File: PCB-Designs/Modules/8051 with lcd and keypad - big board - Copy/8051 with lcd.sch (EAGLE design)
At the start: 45 parts, among them IC1 AT89S51, IC2 7805TV

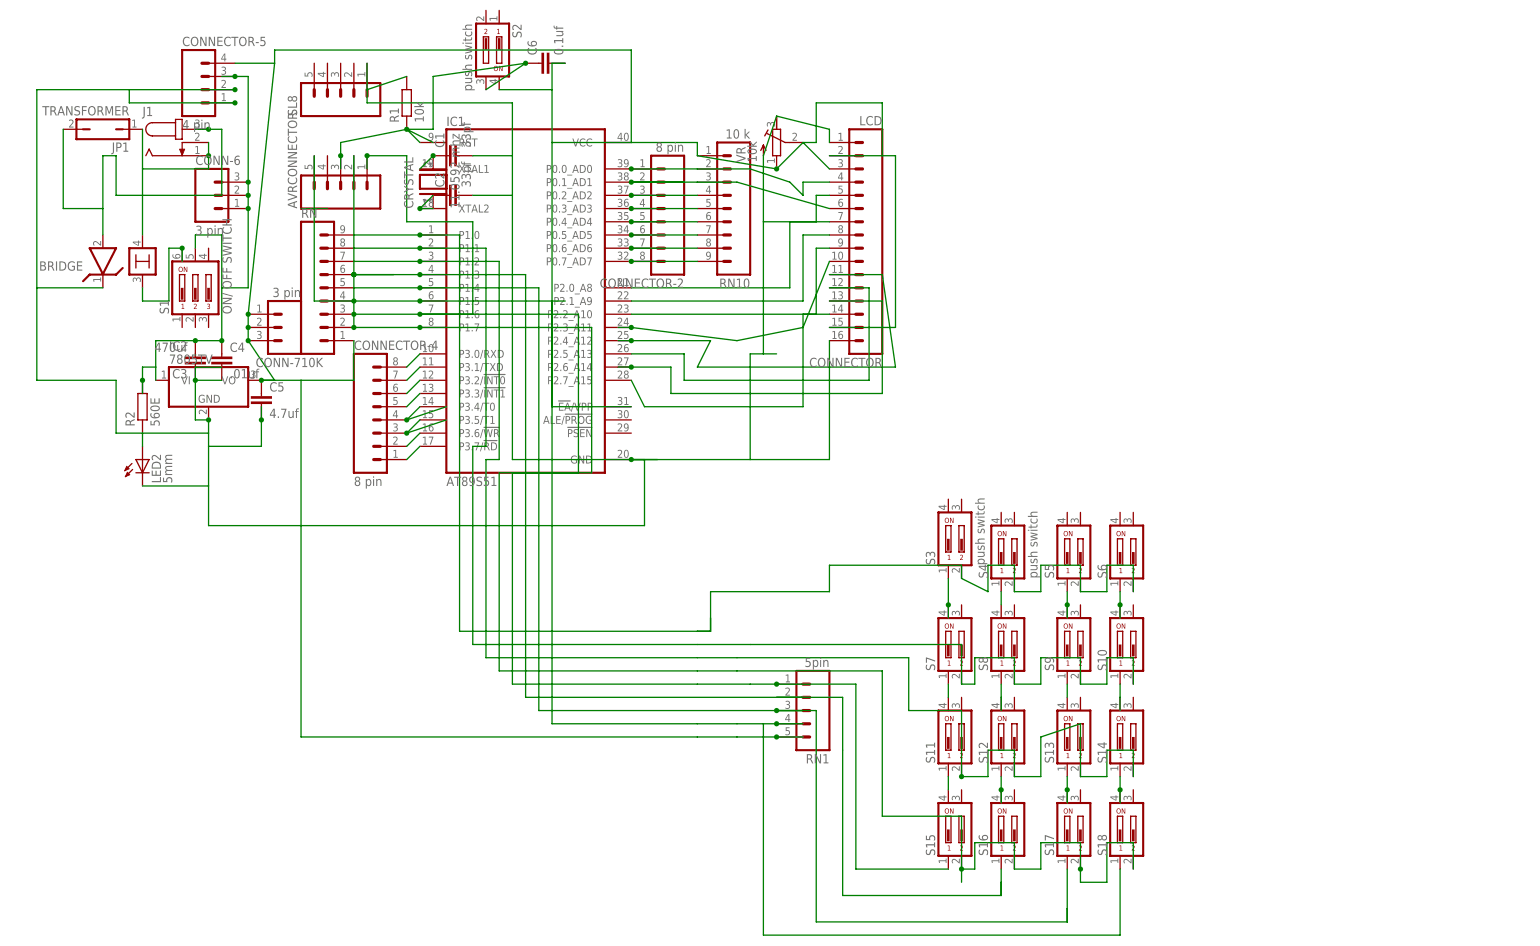
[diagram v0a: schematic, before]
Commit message: 
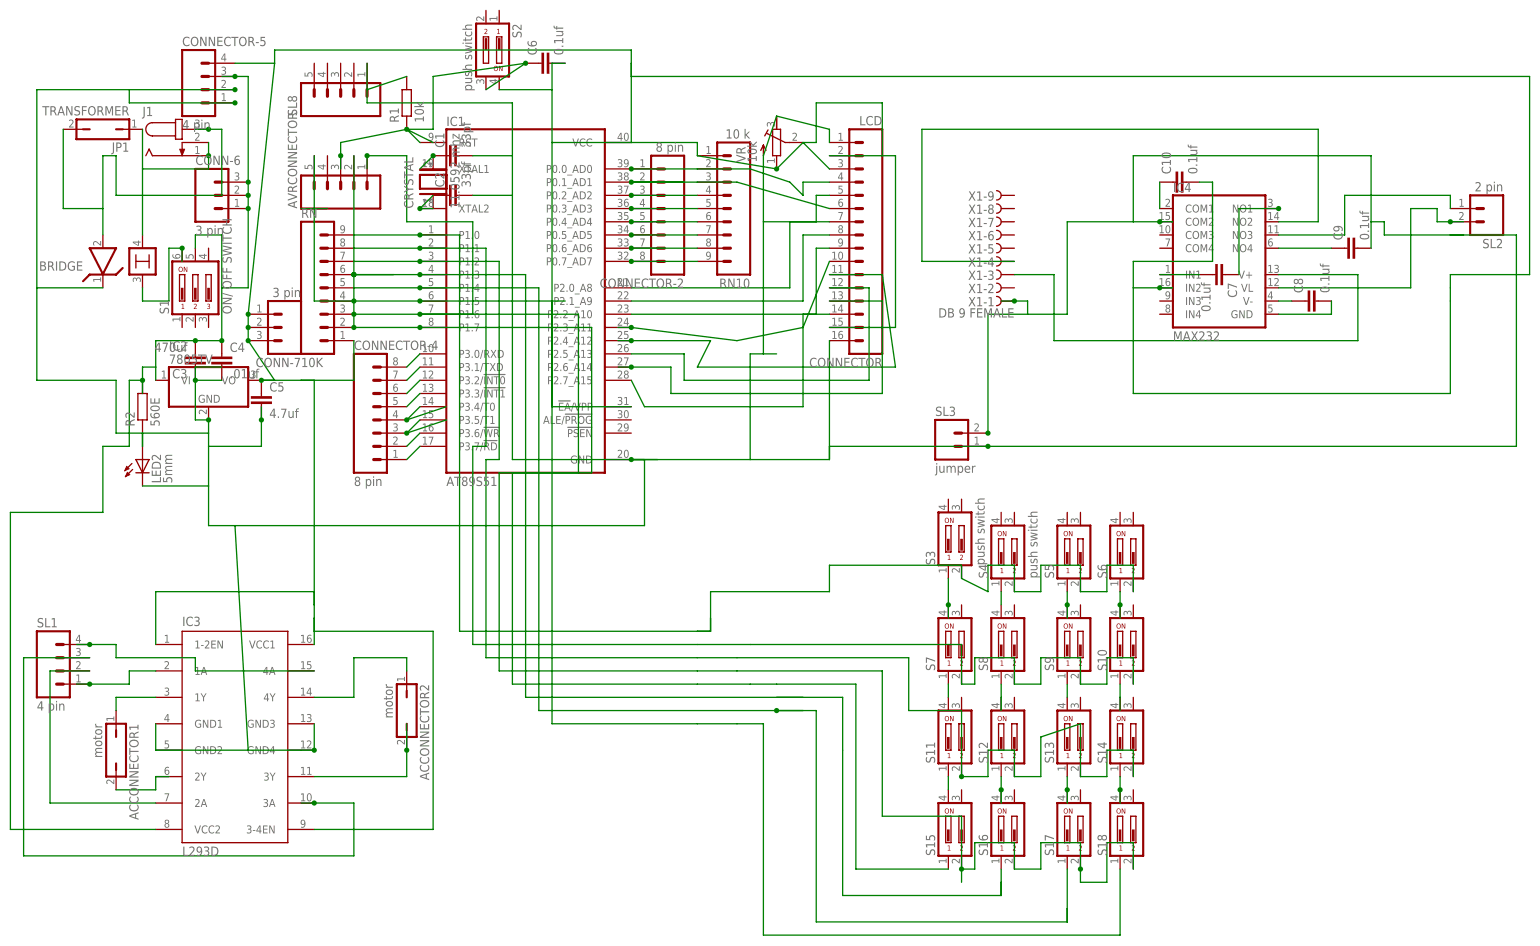
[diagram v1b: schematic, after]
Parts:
- removed RN1: 5pin, con-amp-quick:M05
- added ACCONNECTOR1, ACCONNECTOR2: motor, jumper:JP1Q
- added C10, C7, C8, C9: 0.1uf, capacitor-wima:C2,5-3
- added IC3: L293D, st-microelectronics:L293D
- added IC4: MAX232, maxim:MAX313EPE
- added SL1: 4 pin, con-amp-quick:M04
- added SL2: 2 pin, con-amp-quick:M02
- added SL3: jumper, con-amp-quick:M02
- added X1: DB 9 FEMALE, con-thomas-betts:D-SUB9-H2M09ST
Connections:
- removed net N$39: C5.1, C6.2, CONN-7.1, CONN-7.2, CONN-7.3, CONNECTOR-5.4, CONNECTOR.15, CONNECTOR.2, IC1.!EA!/VPP, IC1.VCC, IC2.VO, RN.1, RN1.5, RN10.1, S2.4, VR.E
- new net N$23: C7.1, IC4.NO1
- new net N$43: C3.2, C4.1, CONN-6.1, CONN-6.2, CONN-6.3, CONNECTOR-5.3, IC2.VI, IC3.VCC2, R2.2, S1.5
- new net N$53: C8.1, IC4.V-
- new net N$57: ACCONNECTOR1.1, IC3.1Y
- new net N$59: ACCONNECTOR1.2, IC3.2Y
- new net N$60: ACCONNECTOR2.1, IC3.4Y
- new net N$61: ACCONNECTOR2.2, IC3.3Y
- new net N$66: IC3.2A, SL1.2
- new net N$67: IC3.3A, SL1.3
- new net N$68: IC3.4A, SL1.4
- new net N$69: C8.2, IC4.GND
- new net N$70: C9.1, IC4.NO4
- new net N$72: BRIDGE.1, C1.2, C2.2, C3.1, C4.2, C5.2, C9.2, CONNECTOR-5.1, CONNECTOR-5.2, CONNECTOR.1, CONNECTOR.16, CONNECTOR.5, IC1.GND, IC2.GND, IC3.GND1, IC3.GND2, IC3.GND3, IC3.GND4, IC4.COM2, LED2.C, R1.2, SL3.1, SL3.2, SL8.1, VR.A, X1-1.F
- new net N$73: C10.1, IC4.COM1
- new net N$74: C10.2, C5.1, C6.2, CONN-7.1, CONN-7.2, CONN-7.3, CONNECTOR-5.4, CONNECTOR.15, CONNECTOR.2, IC1.!EA!/VPP, IC1.VCC, IC2.VO, IC3.1-2EN, IC3.3-4EN, IC3.VCC1, IC4.IN2, RN.1, RN10.1, S2.4, VR.E
- new net N$75: IC4.V+, X1-3.F
- new net N$76: IC4.NO2, X1-4.F
- new net N$77: IC4.NO3, SL2.1
- new net N$78: IC4.VL, SL2.2
- net N$17: no longer RN1.1
- net N$22: no longer RN1.2
- net N$4: now also C7.2, IC4.IN1; no longer C3.2, C4.1, CONN-6.1, CONN-6.2, CONN-6.3, CONNECTOR-5.3, IC2.VI, R2.2, S1.5
- net N$41: now also IC3.1A, SL1.1; no longer BRIDGE.1, C1.2, C2.2, C3.1, C4.2, C5.2, CONNECTOR-5.1, CONNECTOR-5.2, CONNECTOR.1, CONNECTOR.16, CONNECTOR.5, IC1.GND, IC2.GND, LED2.C, R1.2, SL8.1, VR.A
- net N$42: no longer RN1.3
- net N$45: no longer RN1.4
